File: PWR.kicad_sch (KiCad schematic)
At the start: 22 parts, among them J1 Conn_01x04_Pin, J2 Conn_01x03_Pin, J3 Conn_01x03_Pin, J4 Conn_01x03_Pin, J5 Conn_01x03_Pin, J6 Conn_01x04_Pin, U1 LM66100DCK, U2 XC6206P332MR

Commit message: feat: added connection for sensors
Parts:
- C1: footprint Capacitor_SMD:C_0805_2012Metric -> Capacitor_SMD:C_0805_2012Metric_Pad1.18x1.45mm_HandSolder
- D1: footprint Diode_SMD:D_SMB -> Diode_SMD:D_SMB_Handsoldering
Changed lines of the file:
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@@
 			)
 		)
-		(property "Footprint" "Capacitor_SMD:C_0805_2012Metric"
+		(property "Footprint" "Capacitor_SMD:C_0805_2012Metric_Pad1.18x1.45mm_HandSolder"
 			(at 175.26 91.44 0)
 			(hide yes)
@@
 			)
 		)
-		(property "Footprint" "Diode_SMD:D_SMB"
+		(property "Footprint" "Diode_SMD:D_SMB_Handsoldering"
 			(at 163.83 90.17 0)
 			(hide yes)

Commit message: feat: firs complete version schemattic
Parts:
- removed J6: Conn_01x04_Pin, Connector_PinSocket_2.54mm:PinSocket_1x04_P2.54mm_Vertical, symbol Connector:Conn_01x04_Pin
- added C29, C30: 0.1u, Capacitor_SMD:C_0805_2012Metric_Pad1.18x1.45mm_HandSolder, symbol Device:C_Small
- added D4: BAT54C, Package_TO_SOT_SMD:SOT-23_Handsoldering, symbol Diode:BAT54C
- added J10: Conn_01x02_Pin, Connector_Hirose:Hirose_DF13-02P-1.25DSA_1x02_P1.25mm_Vertical, symbol Connector:Conn_01x02_Pin
- added R10: 1k, Resistor_SMD:R_0805_2012Metric_Pad1.20x1.40mm_HandSolder, symbol Device:R
- added R11: 10k, Resistor_SMD:R_0805_2012Metric_Pad1.20x1.40mm_HandSolder, symbol Device:R
- added R9: 3k, Resistor_SMD:R_0805_2012Metric_Pad1.20x1.40mm_HandSolder, symbol Device:R
- added U4: MCP6001-OT, Package_TO_SOT_SMD:SOT-23-5, symbol Amplifier_Operational:MCP6001-OT
- added VD4, VD5, VD6, VD7, VD8: GSOT03C-E3-08, Package_TO_SOT_SMD:SOT-23_Handsoldering, symbol TWS:GSOT03C-E3-08
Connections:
- net +3V3A: now also C30.1, U4.5 (V+)
- net GND: now also C29.2, C30.2, J10.2 (Pin_2), R10.2, U4.2 (V-), VD4.3 (A), VD5.3 (A), VD6.3 (A), VD7.3 (A), VD8.3 (A)
- net PWM1: now also VD5.1 (K1), VD5.2 (K2)
- net PWM2: now also VD6.1 (K1), VD6.2 (K2)
- net PWM3: now also VD7.1 (K1), VD7.2 (K2)
- net PWM4: now also VD8.1 (K1), VD8.2 (K2)
- new net: R10.1, R11.1, R9.2, VD4.1 (K1), VD4.2 (K2)
- new net: C29.1, R11.2, U4.3 (+)
- new net: D4.3, R9.1
- new net: D4.1, J10.1 (Pin_1)
- new net BAT_CTRL: U4.1, U4.4 (-)
- no-connect marks 0 -> 1
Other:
- moved on the sheet: C1, C10, C11, C2, C3, C4, C5, C6, C7, C8, C9, D1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

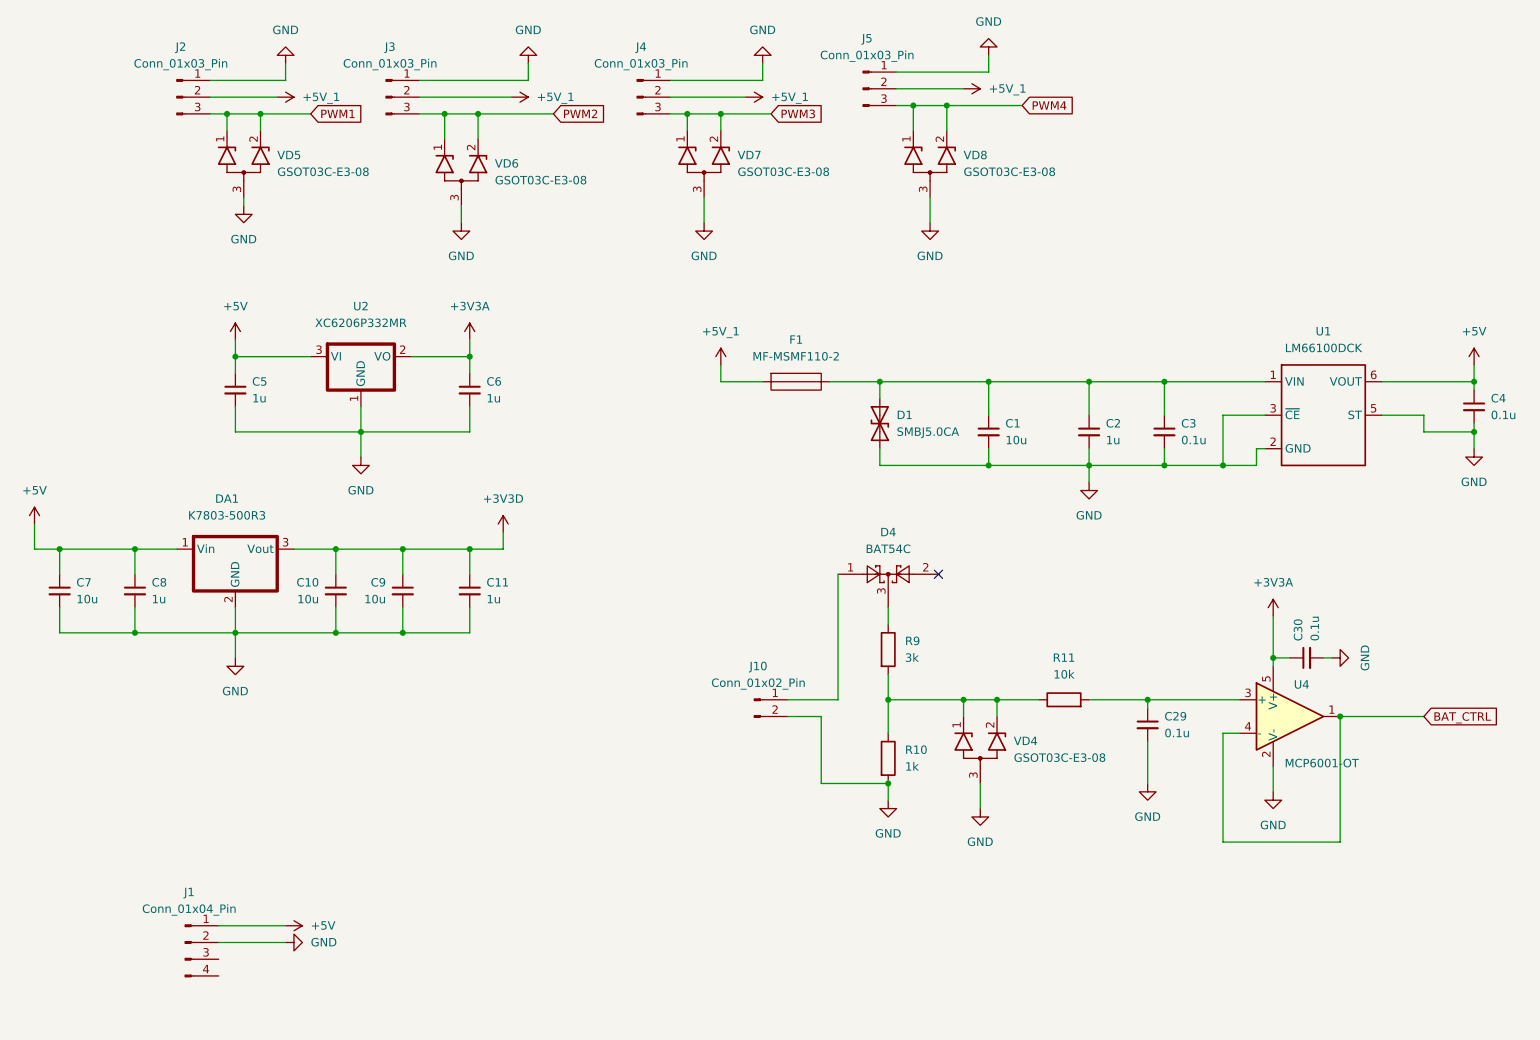
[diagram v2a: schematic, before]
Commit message: feat: added UART for debug
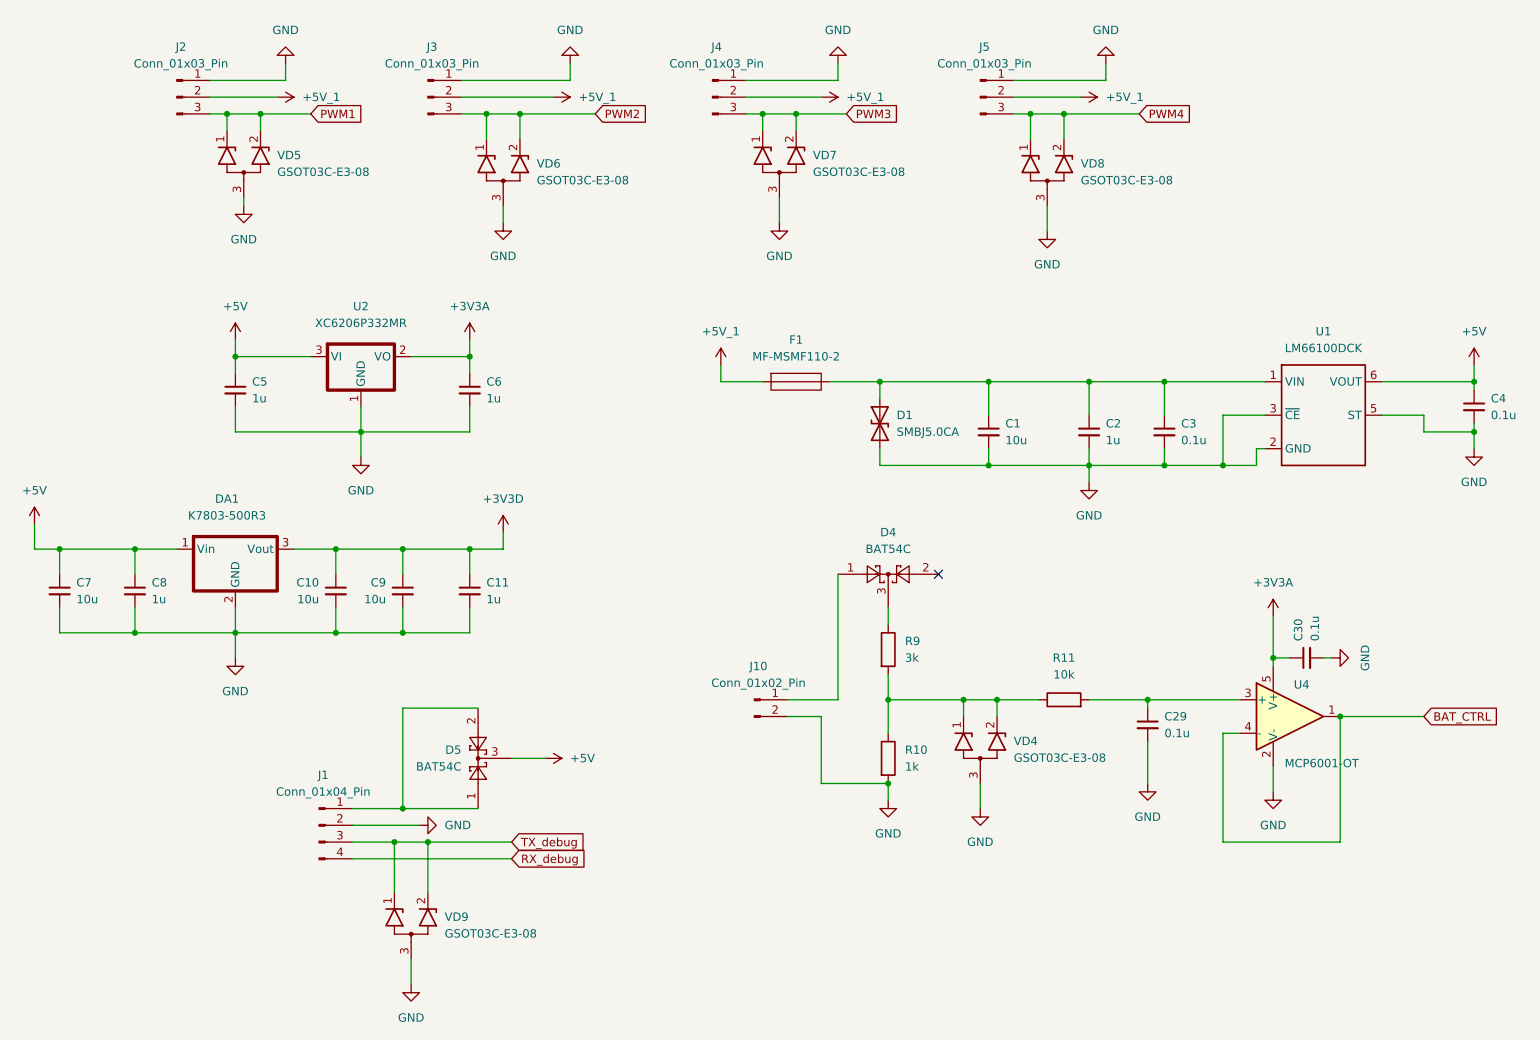
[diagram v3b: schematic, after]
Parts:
- added D5: BAT54C, Package_TO_SOT_SMD:SOT-23_Handsoldering, symbol Diode:BAT54C
- added VD9: GSOT03C-E3-08, Package_TO_SOT_SMD:SOT-23_Handsoldering, symbol TWS:GSOT03C-E3-08
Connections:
- net +5V: now also D5.3; no longer J1.1 (Pin_1)
- net GND: now also VD9.3 (A)
- net TX_debug: now reaches J1.3 (Pin_3)
- net TX_debug: now also VD9.1 (K1), VD9.2 (K2)
- net RX_debug: now reaches J1.4 (Pin_4)
- new net: D5.1, D5.2, J1.1 (Pin_1)
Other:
- moved on the sheet: J1, J3, J4, J5, VD6, VD7, VD8
